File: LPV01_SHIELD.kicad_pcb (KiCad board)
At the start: 4 copper layers, 88 x 118 mm, 147 parts, among them J1 GPIO_header, J10 Screw_Terminal_01x02, J11 PWR_input, J2 PWR_socket, J3 SPI_header, J4 Relay_PWR_in, J5 Conn_01x02_Pin, J6 Relay_PWR, J7 Wiegand, J8 Inputs, J9 Inputs, Q1 BC817, Q101 TLP521-4XSM, Q102 TLP521-4XSM, Q103 TLP521-4XSM, Q104 TLP521-4XSM, Q2 BC817, Q3 BC817, Q4 BC817, Q5 BC817, Q6 BC817, Q7 BC817, Q8 BC817, SW1 SW_SPST, SW2 SW_SPST, SW3 SW_SPST, SW4 SW_SPST, SW5 SW_SPST, SW6 SW_SPST, SW7 SW_SPST, SW8 SW_SPST, U1 MP2491C

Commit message: Made the PCK the size of the LP board
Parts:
- removed Q101, Q102, Q103, Q104: TLP521-4XSM, SamacSys_Parts:TLP5214XSM
- removed SW1, SW2, SW3, SW4, SW5, SW6, SW7, SW8: SW_SPST, Button_Switch_SMD:SW_SPST_CK_RS282G05A3
- added U2: TCMT4100, Package_SO:SOP-16_4.4x10.4mm_P1.27mm, F.Cu at (64.2, 53.6)
- added U3: TCMT4100, Package_SO:SOP-16_4.4x10.4mm_P1.27mm, F.Cu at (76.6, 53.6)
- added U4: TCMT4100, Package_SO:SOP-16_4.4x10.4mm_P1.27mm, F.Cu at (92.6, 58.5)
- added U5: TCMT4100, Package_SO:SOP-16_4.4x10.4mm_P1.27mm, F.Cu at (110.0, 58.5)
- H1, H2, H3, H4: footprint MountingHole:MountingHole_3.2mm_M3_DIN965_Pad -> MountingHole:MountingHole_3.2mm_M3_DIN965
- R34: value 10k -> -> 10k
- moved J6 148.6 mm to (18.5, 3.62)
- moved J4 136.6 mm to (9.43, 3.62)
- moved H2 132.6 mm to (3.08, 10.2)
- moved J5 123.0 mm to (8.97, 11.5), turned to 0 degrees
- moved H1 77.5 mm to (3.08, 3.08)
- moved J10 62.9 mm to (133.2, 68.2)
- moved D1 55.7 mm to (61.1, 64.8)
- moved Q1 55.7 mm to (67.1, 65.0)
- moved R10 55.7 mm to (67.1, 62.4)
- moved D2 55.7 mm to (63.6, 63.4)
- moved R11 55.7 mm to (61.1, 61.9)
- moved R9 55.7 mm to (67.1, 60.9)
- moved D3 55.4 mm to (70.1, 64.8)
- moved Q2 55.4 mm to (76.1, 65.0)
- moved R13 55.4 mm to (76.1, 62.4)
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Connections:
- J11 pad 1: GND -> +24V
- J11 pad 2: +24V -> GND
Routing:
- net Net-(J9-Pin_8): track 61.2 -> 0.00 mm
- net /O8: track 60.7 -> 1.48 mm, vias 2 -> 0
- net /O7: track 58.8 -> 1.48 mm, vias 2 -> 0
- net /O6: track 53.9 -> 1.48 mm, vias 2 -> 0
- net Net-(D18-K): track 52.0 -> 0.00 mm, vias 4 -> 0
- net Net-(J9-Pin_7): track 48.4 -> 0.00 mm
- net /O5: track 49.0 -> 1.48 mm, vias 2 -> 0
- net Net-(D19-K): track 39.1 -> 0.00 mm, vias 4 -> 0
- net Net-(J9-Pin_6): track 35.7 -> 0.00 mm
- net D12: track 75.8 -> 42.6 mm
- net Net-(R4-Pad1): track 0.09 -> 32.2 mm
- net Net-(R3-Pad1): track 0.07 -> 32.1 mm
- net Net-(R2-Pad1): track 0.12 -> 31.5 mm
- net D19: track 94.9 -> 63.6 mm
- net Net-(J9-Pin_4): track 31.1 -> 0.00 mm
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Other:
- board size 88 x 118 mm -> 88 x 85 mm
- board text added: "1"
- board text removed: "IN1"
- board text removed: "IN2"
- board text removed: "IN3"
- board text removed: "IN4"
- board text removed: "IN5"
- board text removed: "IN6"
- board text removed: "IN7"
- board text removed: "IN8"
- board text removed: "INPUT"
- board text removed: "OUT 1"
- board text removed: "OUT 2"
- board text removed: "OUT 3"
- board text removed: "OUT 4"
- board text removed: "OUT 5"
- board text removed: "OUT 6"
- board text removed: "OUT 7"
- board text removed: "OUT 8"
- board text removed: "OUT1"
- board text removed: "OUT2"
- board text removed: "OUT3"
- board text removed: "OUT4"
- board text removed: "OUT5"
- board text removed: "OUT6"
- board text removed: "OUT7"
- board text removed: "OUT8"
- board text removed: "OUTPUT"
- board text removed: "VR"

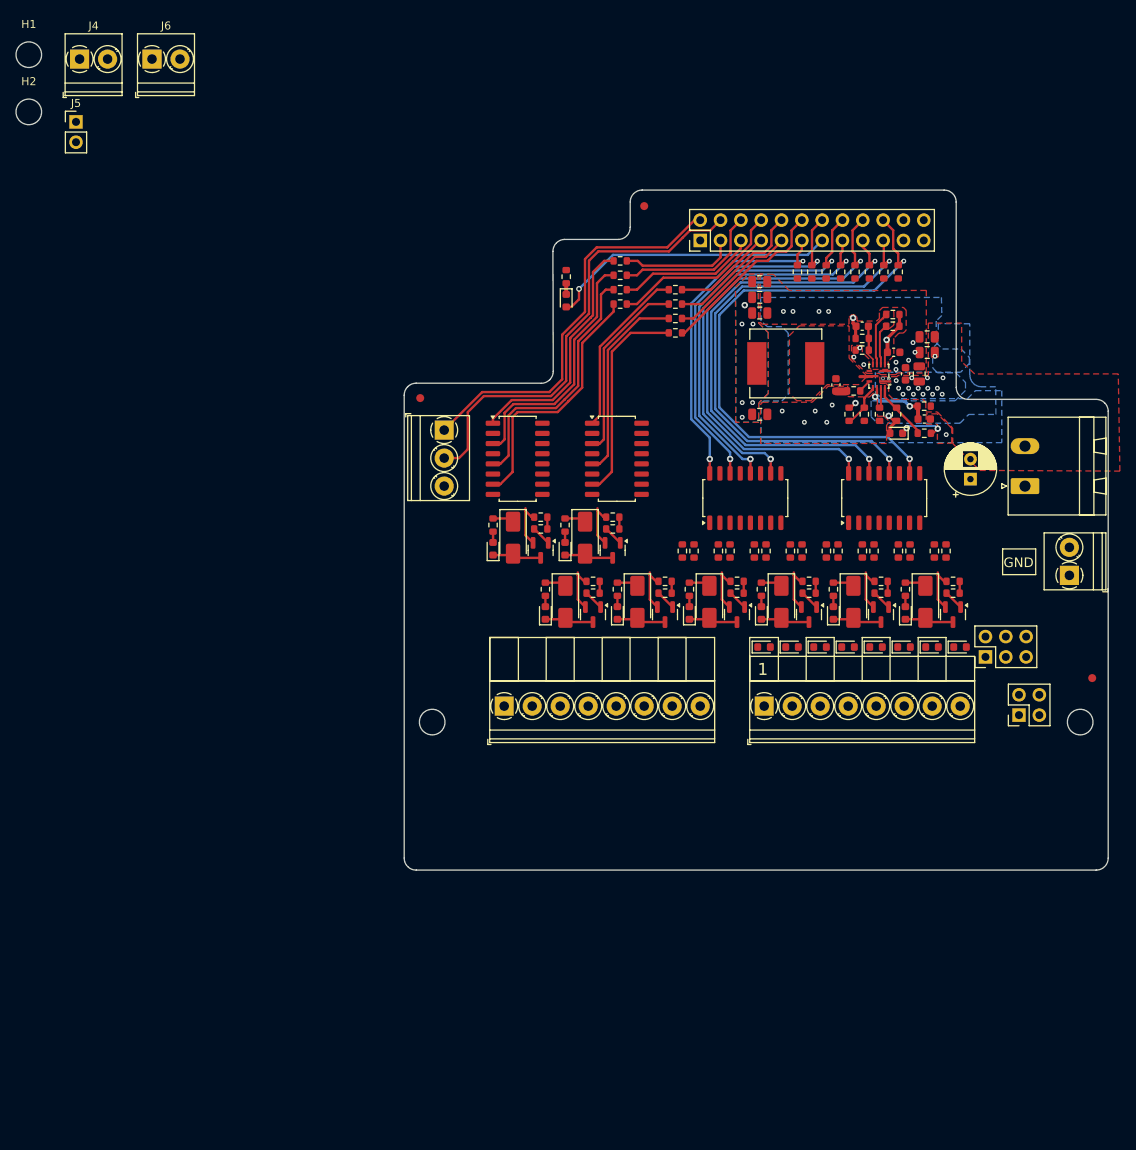
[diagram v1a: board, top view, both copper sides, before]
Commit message: PCB shortened to final measurements
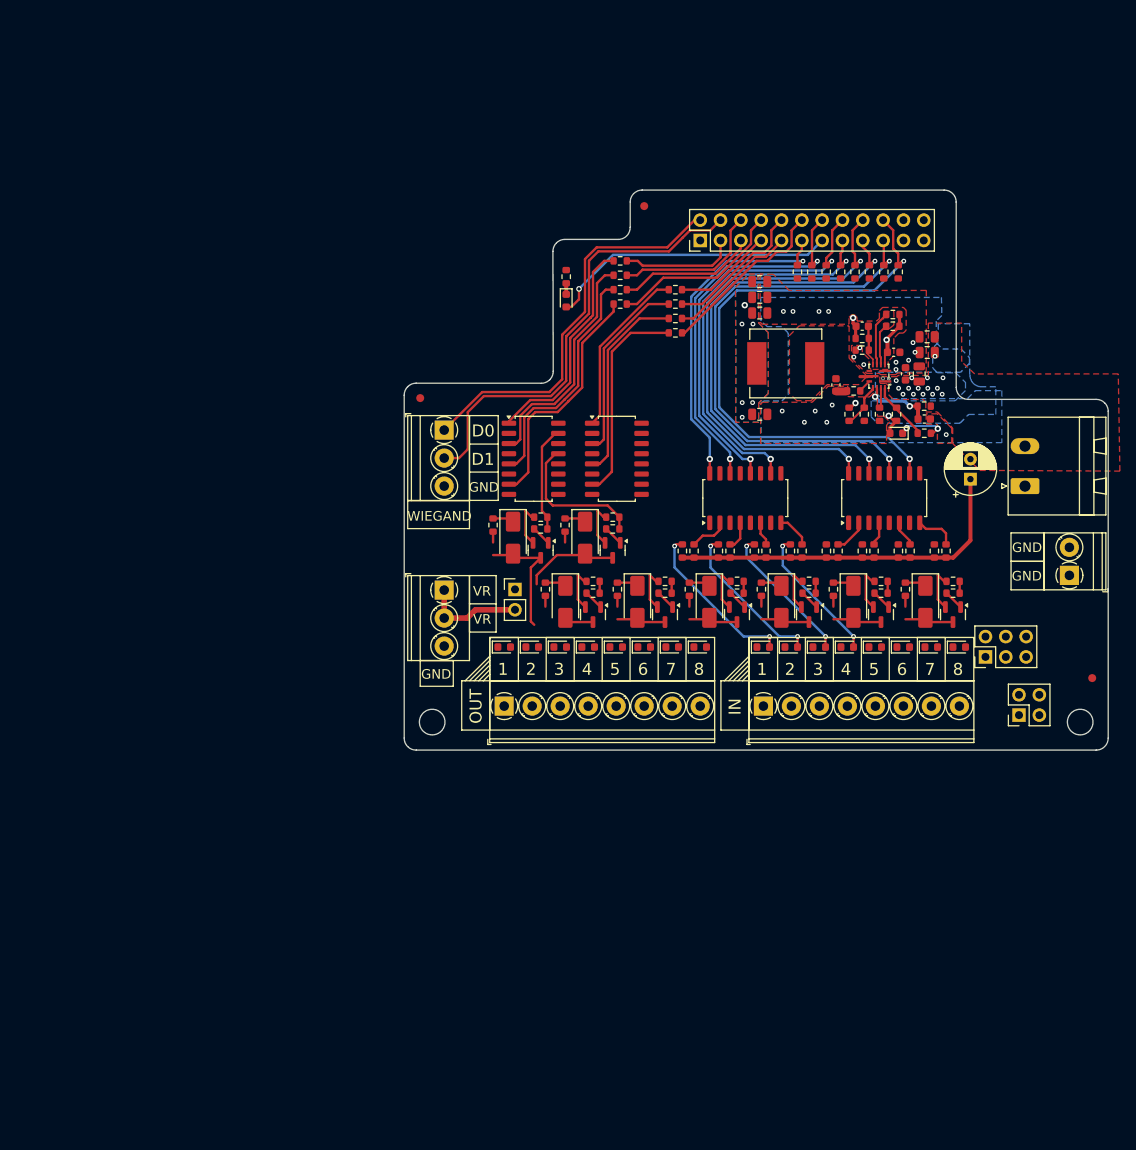
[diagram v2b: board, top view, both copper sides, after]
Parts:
- removed the H1 at (3.08, 3.08)
- removed the H2 at (3.08, 10.2)
- removed the J6 at (18.5, 3.62)
- J4: value Relay_PWR_in -> Wiegand; footprint TerminalBlock_Phoenix:TerminalBlock_Phoenix_PT-1,5-2-3.5-H_1x02_P3.50mm_Horizontal -> TerminalBlock_Phoenix:TerminalBlock_Phoenix_PT-1,5-3-3.5-H_1x03_P3.50mm_Horizontal
- moved J4 80.5 mm to (55.0, 70.0), turned to -90 degrees
- moved J5 80.2 mm to (63.9, 69.9)
- moved D15 26.0 mm to (87.0, 77.1), turned to 0 degrees
- moved D13 20.6 mm to (83.5, 77.1), turned to 0 degrees
- moved D11 15.3 mm to (80.0, 77.1), turned to 0 degrees
- moved D3 13.0 mm to (66.0, 77.1), turned to 0 degrees
- moved D1 12.4 mm to (62.5, 77.1), turned to 0 degrees
- moved D9 10.1 mm to (76.5, 77.1), turned to 0 degrees
- moved D7 5.61 mm to (73.0, 77.1), turned to 0 degrees
- moved D5 4.64 mm to (69.5, 77.1), turned to 0 degrees
- moved U2 2.00 mm to (66.2, 53.6)
- moved D18 0.10 mm to (94.9, 77.1)
- moved D19 0.10 mm to (98.4, 77.1)
- moved D20 0.10 mm to (101.9, 77.1)
- moved D21 0.10 mm to (105.4, 77.1)
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- renumbered H3 to H1, H4 to H2, J7 to J6
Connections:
- J4 pad 2: GND -> VR
- R34 pad 2: Net-(J9-Pin_8) -> Net-(J9-Pin_1)
- R35 pad 2: Net-(J9-Pin_7) -> Net-(J9-Pin_2)
- R36 pad 2: Net-(J9-Pin_6) -> Net-(J9-Pin_3)
- R37 pad 2: Net-(J9-Pin_5) -> Net-(J9-Pin_4)
- R38 pad 2: Net-(J9-Pin_4) -> Net-(J9-Pin_5)
- R39 pad 2: Net-(J9-Pin_3) -> Net-(J9-Pin_6)
- R40 pad 2: Net-(J9-Pin_2) -> Net-(J9-Pin_7)
- R41 pad 2: Net-(J9-Pin_1) -> Net-(J9-Pin_8)
- U4 pad 1: Net-(D21-K) -> Net-(D18-K)
- U4 pad 2: Net-(J9-Pin_5) -> Net-(J9-Pin_1)
- U4 pad 3: Net-(D20-K) -> Net-(D19-K)
- U4 pad 4: Net-(J9-Pin_6) -> Net-(J9-Pin_2)
- U4 pad 5: Net-(D19-K) -> Net-(D20-K)
- U4 pad 6: Net-(J9-Pin_7) -> Net-(J9-Pin_3)
- U4 pad 7: Net-(D18-K) -> Net-(D21-K)
- U4 pad 8: Net-(J9-Pin_8) -> Net-(J9-Pin_4)
- U5 pad 2: Net-(J9-Pin_4) -> Net-(J9-Pin_5)
- U5 pad 4: Net-(J9-Pin_3) -> Net-(J9-Pin_6)
- U5 pad 6: Net-(J9-Pin_2) -> Net-(J9-Pin_7)
- U5 pad 8: Net-(J9-Pin_1) -> Net-(J9-Pin_8)
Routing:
- net +24V: track 0.00 -> 44.6 mm
- net Net-(D18-A): track 0.00 -> 20.5 mm, vias 0 -> 2
- net Net-(D19-A): track 0.00 -> 19.5 mm, vias 0 -> 2
- net Net-(D20-A): track 0.00 -> 17.8 mm, vias 0 -> 2
- net Net-(D21-A): track 0.00 -> 17.4 mm, vias 0 -> 2
- net /O2: track 1.48 -> 18.1 mm
- net VR: track 21.3 -> 34.1 mm
- net /O1: track 1.48 -> 13.3 mm
- net /OUT1: track 6.24 -> 15.3 mm
- net /OUT2: track 6.24 -> 12.0 mm
- net Net-(J9-Pin_8): track 0.00 -> 5.22 mm
- net Net-(J9-Pin_1): track 0.00 -> 4.87 mm
- net Net-(J9-Pin_4): track 0.00 -> 4.30 mm
- net Net-(J9-Pin_5): track 0.00 -> 4.25 mm
- net Net-(J9-Pin_2): track 0.00 -> 3.56 mm
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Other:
- board size 88 x 85 mm -> 88 x 70 mm
- board text added: "2"
- board text added: "3"
- board text added: "4"
- board text added: "5"
- board text added: "6"
- board text added: "7"
- board text added: "8"
- board text added: "D0"
- board text added: "D1"
- board text added: "IN"
- board text added: "OUT"
- board text added: "VR"
- board text added: "WIEGAND"

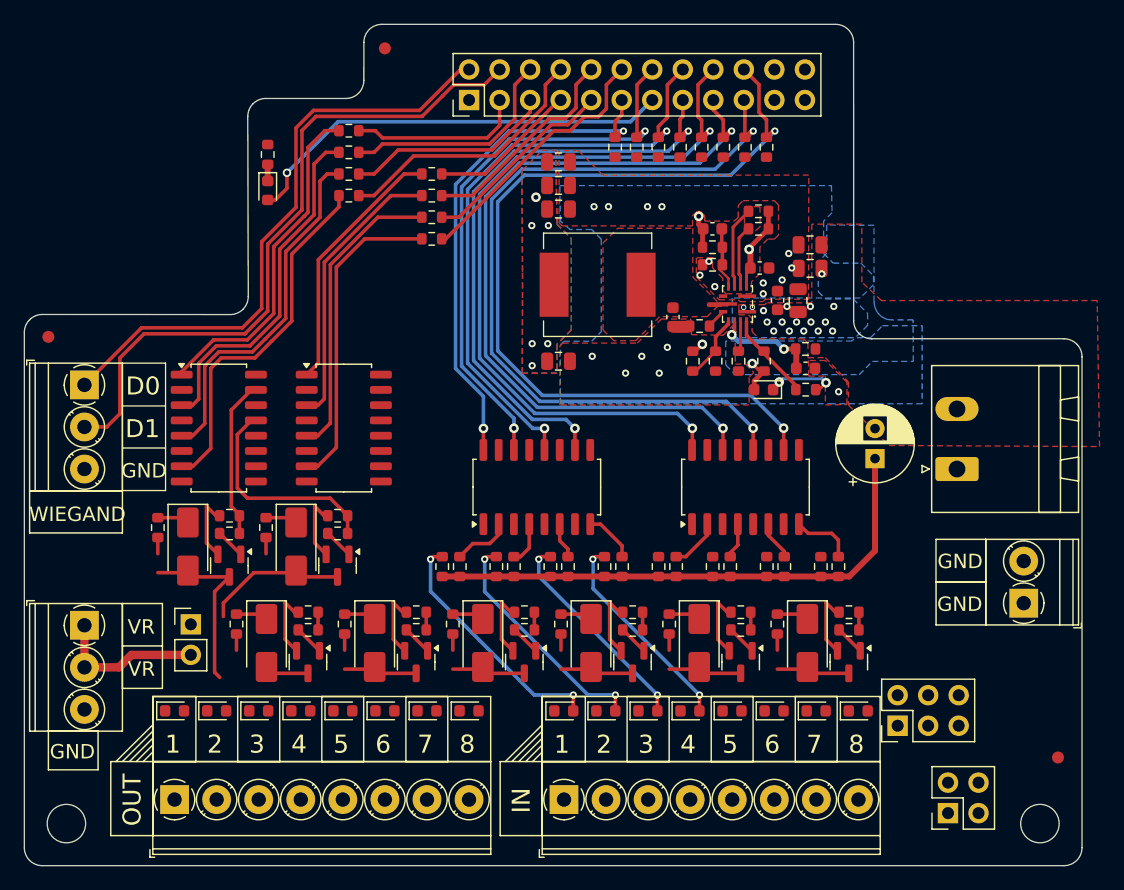
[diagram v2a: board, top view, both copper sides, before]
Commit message: Making fields of copper
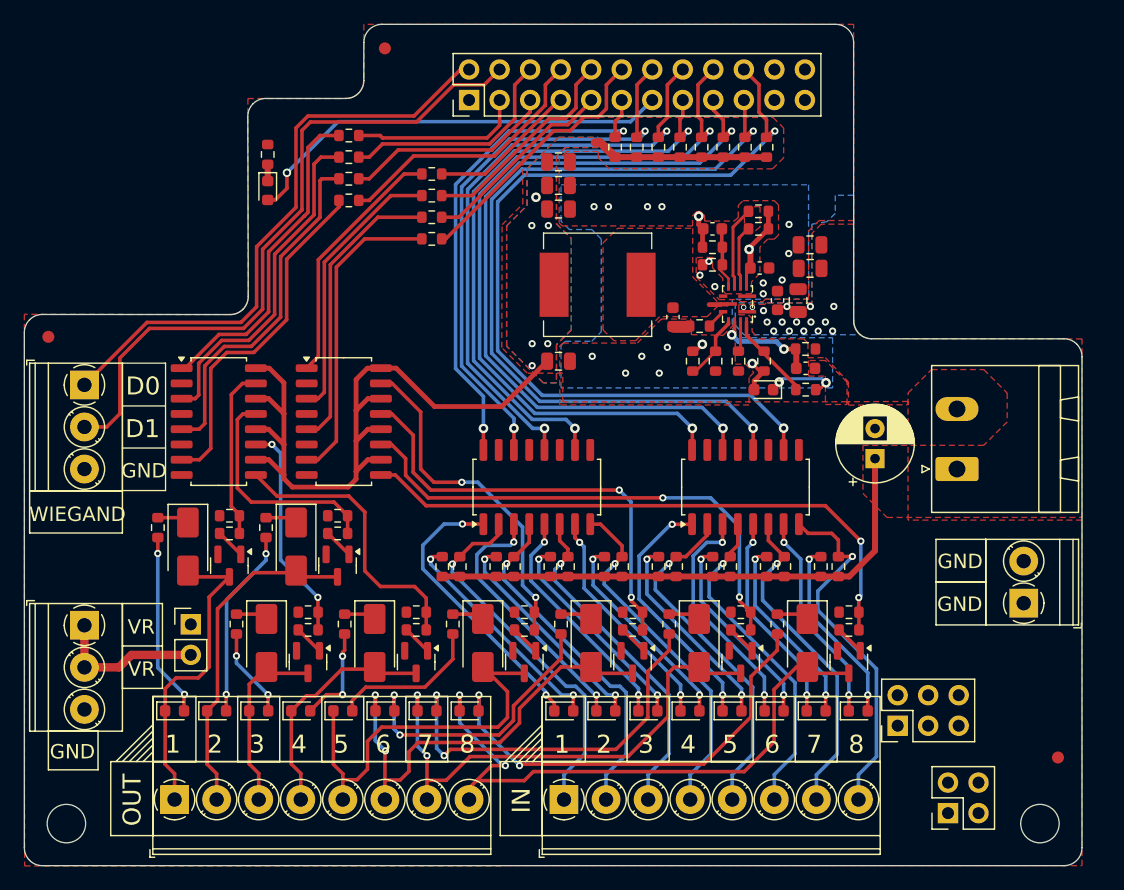
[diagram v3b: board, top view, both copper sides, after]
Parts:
- moved U2 0.54 mm to (66.2, 53.0)
- moved U3 0.54 mm to (76.6, 53.0)
- moved R2 0.40 mm to (77.0, 31.1)
- moved R1 0.40 mm to (77.0, 29.2)
- moved R3 0.40 mm to (77.0, 32.9)
- moved R4 0.40 mm to (77.0, 34.6)
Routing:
- net +5V: track 16.9 -> 92.6 mm
- net /O8: track 1.48 -> 49.7 mm, vias 0 -> 2
- net GND: track 46.5 -> 0.00 mm, vias 19 -> 17
- net /OUT8: track 6.24 -> 51.6 mm, vias 0 -> 2
- net /O7: track 1.48 -> 42.5 mm, vias 0 -> 2
- net /OUT7: track 6.24 -> 42.9 mm, vias 0 -> 2
- net Net-(D15-A): track 1.35 -> 37.4 mm, vias 0 -> 2
- net /O6: track 1.48 -> 36.7 mm, vias 0 -> 2
- net Net-(D13-A): track 1.35 -> 32.6 mm, vias 0 -> 2
- net /OUT6: track 6.24 -> 37.0 mm, vias 0 -> 2
- net /OUT5: track 6.24 -> 33.9 mm
- net /O5: track 1.48 -> 28.6 mm, vias 0 -> 2
- net Net-(J9-Pin_1): track 4.87 -> 31.1 mm, vias 0 -> 1
- net Net-(J9-Pin_2): track 3.56 -> 29.2 mm, vias 0 -> 1
- net Net-(J9-Pin_3): track 2.99 -> 28.3 mm, vias 0 -> 1
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
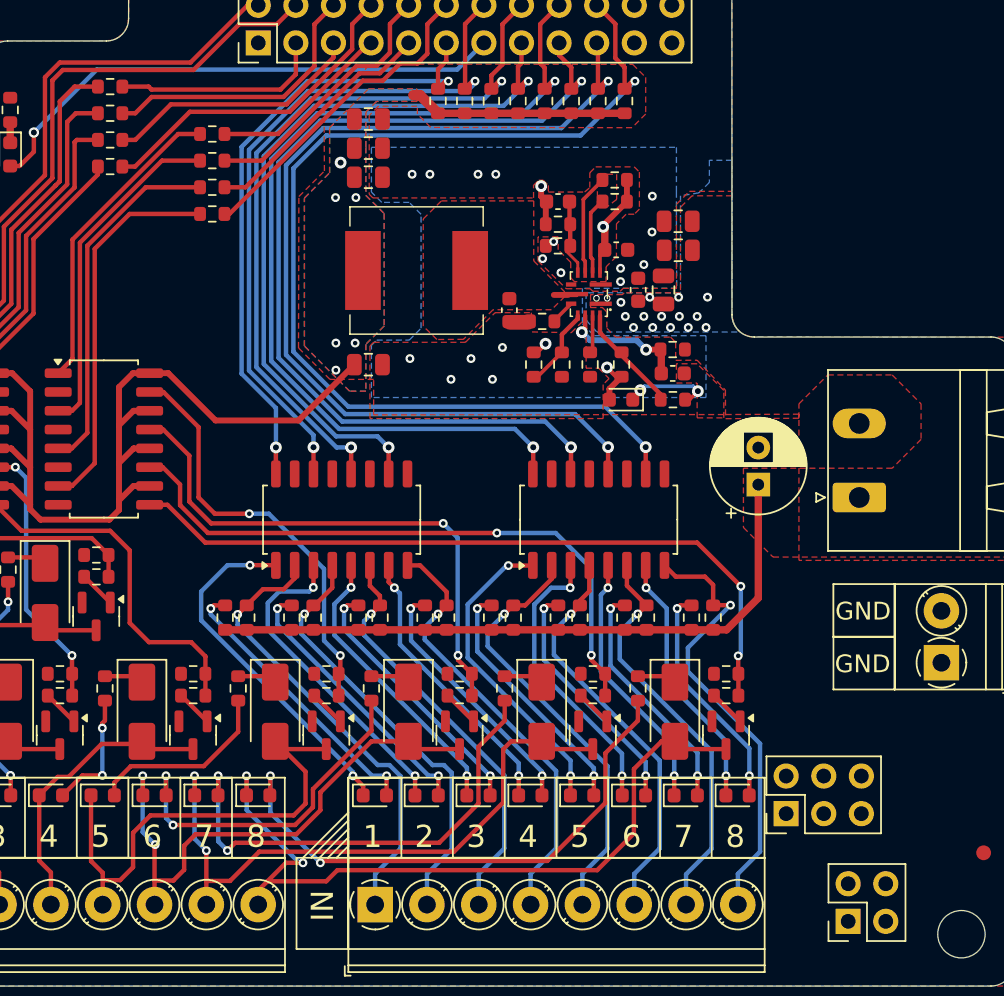
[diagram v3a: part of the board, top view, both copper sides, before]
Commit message: Small adjustments to traces near OUT
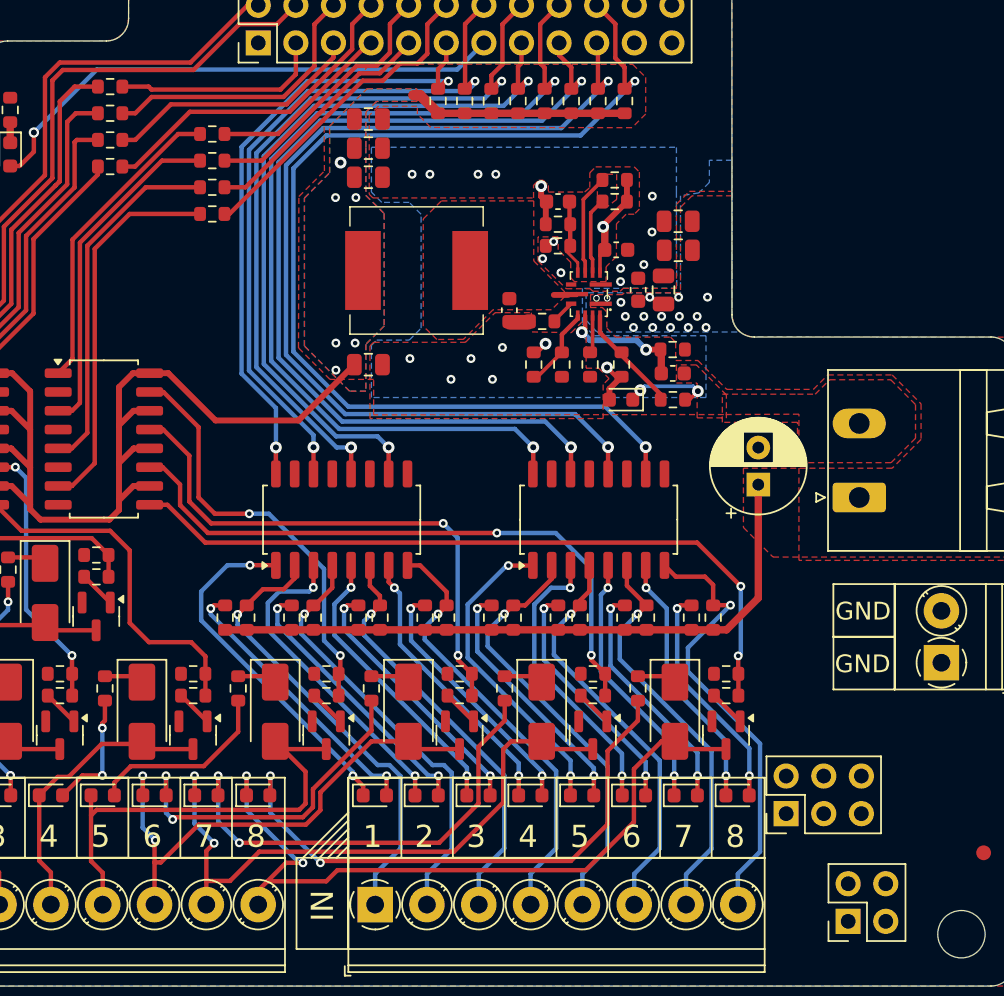
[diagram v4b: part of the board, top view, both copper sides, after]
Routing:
- net /OUT5: track 33.9 -> 31.5 mm
- net /OUT6: track 37.0 -> 35.6 mm
- net Net-(D13-A): track 32.6 -> 31.4 mm
- net Net-(D15-A): track 37.4 -> 38.3 mm
- net Net-(D11-A): track 23.6 -> 23.1 mm
